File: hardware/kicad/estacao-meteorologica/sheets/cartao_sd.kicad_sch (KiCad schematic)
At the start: 7 parts, among them J17 Micro_SD_Card, U11 74LVC125

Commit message: refatoracao: atualizacoes de hardware e falta revisao LoRa
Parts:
- removed C9: 10u, symbol Device:C_Polarized
- added C7: 10u / 50V, Capacitor_SMD:C_1206_3216Metric, symbol Device:C
- added C9: 100n, Capacitor_SMD:C_0603_1608Metric, symbol Device:C
- added U39: EMIF06-MSD02N16, Hardware_SD:QFN-16L_L3.5-W1.2-P0.40_EMIF06-MSD02N16, symbol Hardware_SD:EMIF06-MSD02N16
- C10, C8: footprint (none) -> Capacitor_SMD:C_0603_1608Metric; LCSC (none) -> C14663; LCSC Part (none) -> C14663; MPN (none) -> CC0603KRX7R9BB104; Manufacturer (none) -> YAGEO; Rating (none) -> X7R; 100 nF; 50 V; ±10 %; 0603
- J17: value Micro_SD_Card -> 104031-0811; MPN (none) -> 104031-0811; Manufacturer (none) -> Molex; Rating (none) -> 10 V; 0.5 A; -25 °C to +85 °C; SMT
- R17, R18: footprint (none) -> Resistor_SMD:R_0603_1608Metric; LCSC (none) -> C25804; LCSC Part (none) -> C25804; MPN (none) -> 0603WAF1002T5E; Manufacturer (none) -> UNI-ROYAL; Rating (none) -> 10 kOhm; ±1 %; 0.1 W; 0603
- U11: value 74LVC125 -> SN74LVC125APWR; LCSC (none) -> C7813; LCSC Part (none) -> C7813; MPN (none) -> SN74LVC125APWR; Manufacturer (none) -> Texas Instruments; Rating (none) -> VCC 1.65 V to 3.6 V; 24 mA; TSSOP-14
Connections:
- net +5V is gone; now on net +3V3: C8.1, U11.14 (VCC)
- net +3V3: now also C7.1, C9.1, U39.16 (VCC), U39.17 (RDAT_VCC); no longer U11.7 (GND)
- net CS_LLS: now also U39.4 (DAT3_IN); no longer J17.2 (DAT3/CD)
- net DI_LLS: now also U39.5 (CMD_IN); no longer J17.3 (CMD)
- net DO_LLS: now also U39.7 (DAT0_IN); no longer J17.7 (DAT0)
- net GND: now also U11.7 (GND), C7.2, C9.2, U39.18 (GND), U39.19 (GND), U39.9 (GND)
- net SCK_LLS: now also U39.6 (CLK_IN); no longer J17.5 (CLK)
- net DAT2: now reaches J17.1 (DAT2)
- net DAT2: now also U39.15 (DAT2_EX)
- net DAT1: now reaches J17.8 (DAT1)
- net DAT1: now also U39.10 (DAT1_EX)
- new net D_CMD_CARD: J17.3 (CMD), U39.13 (CMD_EX)
- new net SD_CLK_CARD: J17.5 (CLK), U39.12 (CLK_EX)
- new net SD_CS_CARD: J17.2 (DAT3/CD), U39.14 (DAT3_EX)
- new net SD_DO_CARD: J17.7 (DAT0), U39.11 (DAT0_EX)
- no-connect marks 2 -> 4
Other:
- moved on the sheet: C8, J17, R17, R18, U11A, U11B, U11C, U11D, U11E

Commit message: refatoracao: lora + Verificacao projeto inteiro
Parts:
- C10, C8, C9: Modelo 3D (none) -> ${KICAD9_3DMODEL_DIR}/Capacitor_SMD.3dshapes/C_0603_1608Met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; Status_Ficha (none) -> Conferido no catalogo em 2026-09-24; verificar estoque ao c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
- C7: Modelo 3D (none) -> ${KICAD9_3DMODEL_DIR}/Capacitor_SMD.3dshapes/C_1206_3216Met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; Status_Ficha (none) -> Conferido no catalogo em 2026-09-24; verificar estoque ao c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
- J17: LCSC (none) -> Nao confirmado; LCSC Part (none) -> Nao confirmado; Modelo 3D (none) -> PENDENTE: ${KICAD9_3DMODEL_DIR}/Connector_Card.3dshapes/mic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; Status_Ficha (none) -> MPN e geometria preservados; fornecimento LCSC nao confirma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
- R17, R18: Modelo 3D (none) -> ${KICAD9_3DMODEL_DIR}/Resistor_SMD.3dshapes/R_0603_1608Metr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; Status_Ficha (none) -> Conferido no catalogo em 2026-09-24; verificar estoque ao c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
- U11: Modelo 3D (none) -> ${KICAD9_3DMODEL_DIR}/Package_SO.3dshapes/TSSOP-14_4.4x5mm_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; Status_Ficha (none) -> Conferido no catalogo em 2026-09-24; verificar estoque ao c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
- U39: Modelo 3D (none) -> ${KIPRJMOD}/../../libraries/Hardware_SD/Hardware_SD.3dshape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; Status_Ficha (none) -> Conferido no catalogo em 2026-09-24; verificar estoque ao c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
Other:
- moved on the sheet: C7, C9

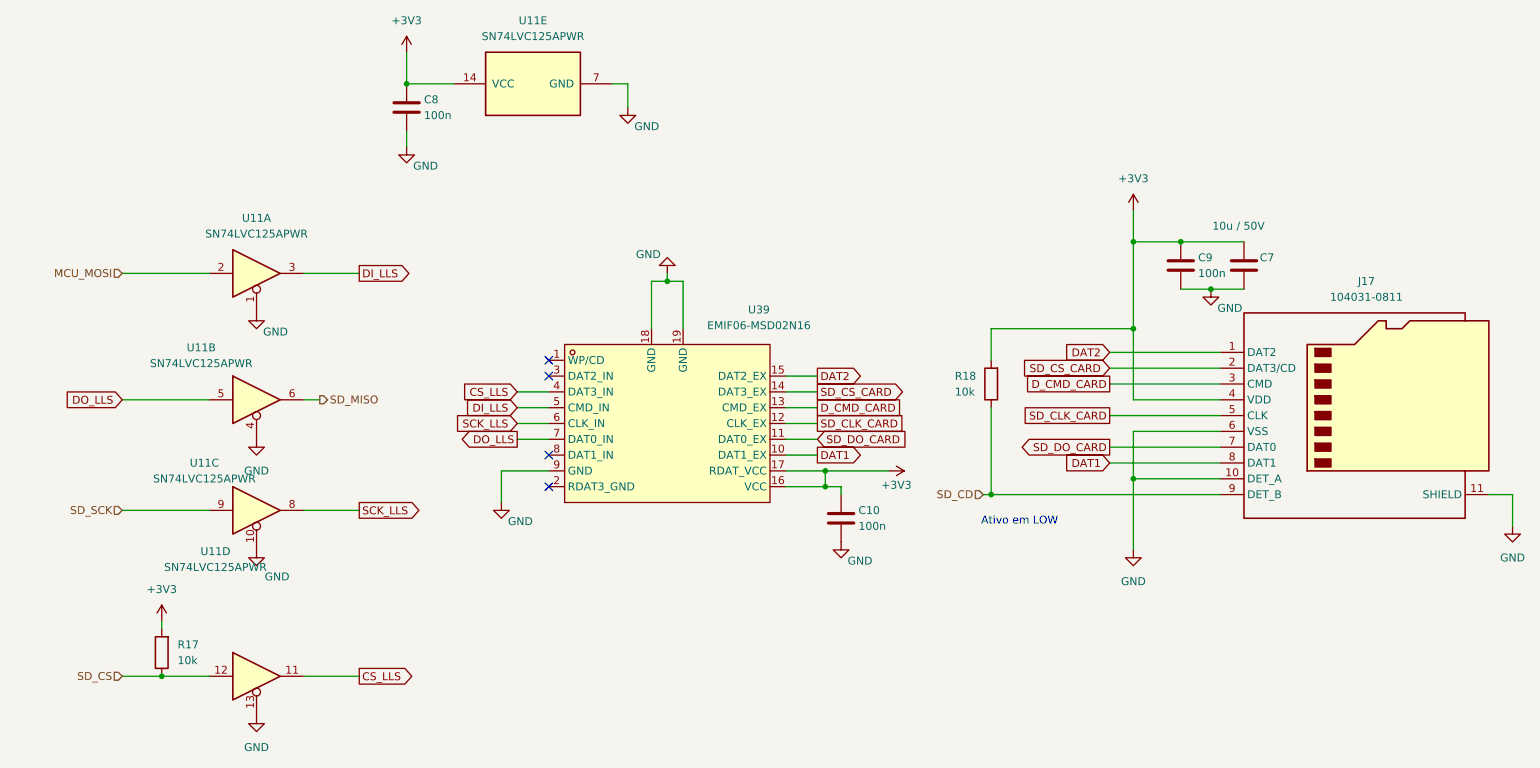
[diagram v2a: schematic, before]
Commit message: Padronizacao de nomes e numero de componentes
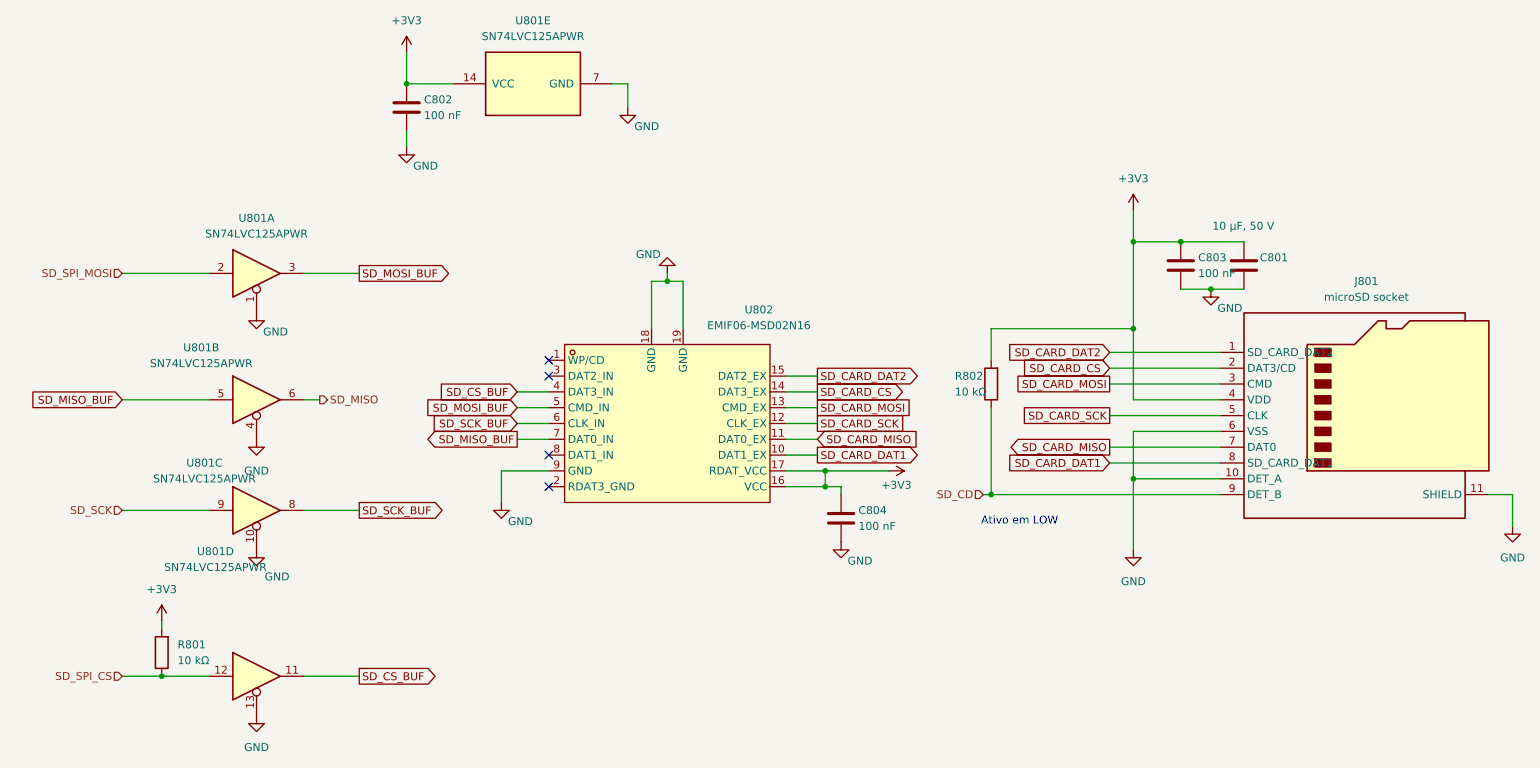
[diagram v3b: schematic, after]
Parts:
- C801: renamed from C7; value 10u / 50V -> 10 µF, 50 V; Assembly (none) -> SMT; Function (none) -> Capacitor de desacoplamento ou filtro local.; LCSC Part C13585 -> (none); Modelo 3D ${KICAD9_3DMODEL_DIR}/Capacitor_SMD.3dshapes/C_1206_3216Met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 -> (none); Rating X5R; 10 uF; 50 V; ±10 %; 1206 -> (none); Specification (none) -> X5R; 10 uF; 50 V; ±10 %; 1206; Status_Ficha Conferido no catalogo em 2026-09-24; verificar estoque ao c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 -> (none); Verification (none) -> Conferido no catalogo em 2026-09-24; verificar estoque ao c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
- C802: renamed from C8; value 100n -> 100 nF; Assembly (none) -> SMT; Function (none) -> Capacitor de desacoplamento ou filtro local.; LCSC Part C14663 -> (none); Modelo 3D ${KICAD9_3DMODEL_DIR}/Capacitor_SMD.3dshapes/C_0603_1608Met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 -> (none); Rating X7R; 100 nF; 50 V; ±10 %; 0603 -> (none); Specification (none) -> X7R; 100 nF; 50 V; ±10 %; 0603; Status_Ficha Conferido no catalogo em 2026-09-24; verificar estoque ao c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 -> (none); Verification (none) -> Conferido no catalogo em 2026-09-24; verificar estoque ao c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
- C803: renamed from C9; value 100n -> 100 nF; Assembly (none) -> SMT; Function (none) -> Capacitor de desacoplamento ou filtro local.; LCSC Part C14663 -> (none); Modelo 3D ${KICAD9_3DMODEL_DIR}/Capacitor_SMD.3dshapes/C_0603_1608Met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 -> (none); Rating X7R; 100 nF; 50 V; ±10 %; 0603 -> (none); Specification (none) -> X7R; 100 nF; 50 V; ±10 %; 0603; Status_Ficha Conferido no catalogo em 2026-09-24; verificar estoque ao c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 -> (none); Verification (none) -> Conferido no catalogo em 2026-09-24; verificar estoque ao c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
- C804: renamed from C10; value 100n -> 100 nF; Assembly (none) -> SMT; Function (none) -> Capacitor de desacoplamento ou filtro local.; LCSC Part C14663 -> (none); Modelo 3D ${KICAD9_3DMODEL_DIR}/Capacitor_SMD.3dshapes/C_0603_1608Met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 -> (none); Rating X7R; 100 nF; 50 V; ±10 %; 0603 -> (none); Specification (none) -> X7R; 100 nF; 50 V; ±10 %; 0603; Status_Ficha Conferido no catalogo em 2026-09-24; verificar estoque ao c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 -> (none); Verification (none) -> Conferido no catalogo em 2026-09-24; verificar estoque ao c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
- J801: renamed from J17; value 104031-0811 -> microSD socket; Assembly (none) -> SMT; Function (none) -> Conector de interface.; LCSC Part Nao confirmado -> (none); Modelo 3D PENDENTE: ${KICAD9_3DMODEL_DIR}/Connector_Card.3dshapes/mic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 -> (none); Rating 10 V; 0.5 A; -25 °C to +85 °C; SMT -> (none); Specification (none) -> 10 V; 0.5 A; -25 °C to +85 °C; SMT; Status_Ficha MPN e geometria preservados; fornecimento LCSC nao confirma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 -> (none); Verification (none) -> MPN e geometria preservados; fornecimento LCSC nao confirma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
- R801: renamed from R17; value 10k -> 10 kΩ; Assembly (none) -> SMT; Function (none) -> Resistor de polarização, filtro ou configuração.; LCSC Part C25804 -> (none); Manufacturer UNI-ROYAL -> UNI-ROYAL(Uniroyal Elec); Modelo 3D ${KICAD9_3DMODEL_DIR}/Resistor_SMD.3dshapes/R_0603_1608Metr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 -> (none); Rating 10 kOhm; ±1 %; 0.1 W; 0603 -> (none); Specification (none) -> 10 kOhm; ±1 %; 0.1 W; 0603; Status_Ficha Conferido no catalogo em 2026-09-24; verificar estoque ao c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 -> (none); Verification (none) -> Conferido no catalogo em 2026-09-24; verificar estoque ao c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
- R802: renamed from R18; value 10k -> 10 kΩ; Assembly (none) -> SMT; Function (none) -> Resistor de polarização, filtro ou configuração.; LCSC Part C25804 -> (none); Manufacturer UNI-ROYAL -> UNI-ROYAL(Uniroyal Elec); Modelo 3D ${KICAD9_3DMODEL_DIR}/Resistor_SMD.3dshapes/R_0603_1608Metr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 -> (none); Rating 10 kOhm; ±1 %; 0.1 W; 0603 -> (none); Specification (none) -> 10 kOhm; ±1 %; 0.1 W; 0603; Status_Ficha Conferido no catalogo em 2026-09-24; verificar estoque ao c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 -> (none); Verification (none) -> Conferido no catalogo em 2026-09-24; verificar estoque ao c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
- U801: renamed from U11; Assembly (none) -> SMT; Function (none) -> Circuito integrado ou módulo funcional.; LCSC Part C7813 -> (none); Modelo 3D ${KICAD9_3DMODEL_DIR}/Package_SO.3dshapes/TSSOP-14_4.4x5mm_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 -> (none); Rating VCC 1.65 V to 3.6 V; 24 mA; TSSOP-14 -> (none); Specification (none) -> VCC 1.65 V to 3.6 V; 24 mA; TSSOP-14; Status_Ficha Conferido no catalogo em 2026-09-24; verificar estoque ao c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 -> (none); Verification (none) -> Conferido no catalogo em 2026-09-24; verificar estoque ao c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
- U802: renamed from U39; 3D Model ${KIPRJMOD}/../../libraries/Hardware_SD/Hardware_SD.3dshape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 -> (none); Assembly (none) -> SMT; Function (none) -> Circuito integrado ou módulo funcional.; LCSC Part C5267594 -> (none); Modelo 3D ${KIPRJMOD}/../../libraries/Hardware_SD/Hardware_SD.3dshape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 -> (none); Rating 6 channels; 45 Ohm series; 20 pF; IEC 61000-4-2 level 4 -> (none); Specification (none) -> 6 channels; 45 Ohm series; 20 pF; IEC 61000-4-2 level 4; Status_Ficha Conferido no catalogo em 2026-09-24; verificar estoque ao c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 -> (none); Verification (none) -> Conferido no catalogo em 2026-09-24; verificar estoque ao c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
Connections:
- net CS_LLS renamed SD_CS_BUF
- net DAT1 renamed SD_CARD_DAT1
- net DAT2 renamed SD_CARD_DAT2
- net DI_LLS renamed SD_MOSI_BUF
- net DO_LLS renamed SD_MISO_BUF
- net D_CMD_CARD renamed SD_CARD_MOSI
- net MCU_MOSI renamed SD_SPI_MOSI
- net SCK_LLS renamed SD_SCK_BUF
- net SD_CLK_CARD renamed SD_CARD_SCK
- net SD_CS renamed SD_SPI_CS
- net SD_CS_CARD renamed SD_CARD_CS
- net SD_DO_CARD renamed SD_CARD_MISO

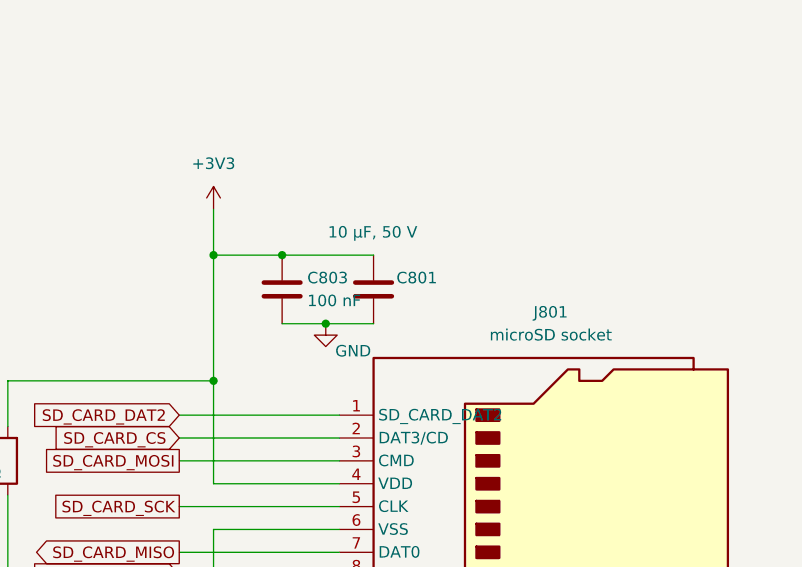
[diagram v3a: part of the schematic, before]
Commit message: Ajuste de componentes por folha
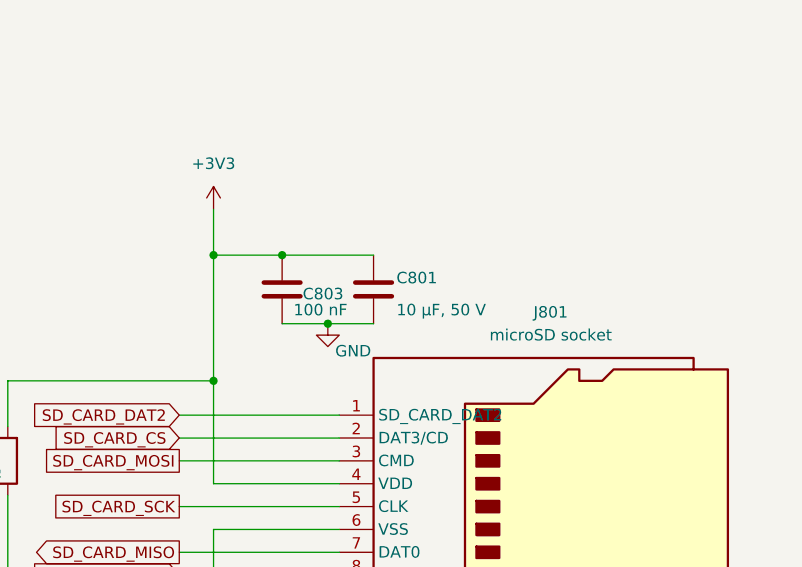
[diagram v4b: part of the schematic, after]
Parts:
- J801: footprint Connector_Card:microSD_HC_Molex_104031-0811 -> Hardware_SD_Interface:microSD_HC_Molex_104031-0811; symbol Connector:Micro_SD_Card_Det2 -> Hardware_SD_Interface:MicroSD_Molex_104031_0811; LCSC Nao confirmado -> C585350; LCSC Part (none) -> C585350; Modelo 3D (none) -> ${KIPRJMOD}/../../libraries/Hardware_SD_Interface/Hardware_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; Verification MPN e geometria preservados; fornecimento LCSC nao confirma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 -> Conferido no catálogo da JLCPCB em 2026-09-25; C585350; con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
- U801: symbol 74xx:74LVC125 -> Hardware_SD_Interface:SN74LVC125APWR

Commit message: Roteamento 1
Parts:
- J801: value microSD socket -> microSD socket, TF-15x15; footprint Hardware_SD_Interface:microSD_HC_Molex_104031-0811 -> Hardware_SD_Interface:microSD_SOFNG_TF-15x15; Function Conector de interface. -> Socket microSD para armazenamento SPI; contatos 1-8 e detec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; LCSC C585350 -> C111196; LCSC Part C585350 -> (none); MPN 104031-0811 -> TF-15x15; Manufacturer Molex -> SOFNG; Modelo 3D ${KIPRJMOD}/../../libraries/Hardware_SD_Interface/Hardware_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 -> (none); Specification 10 V; 0.5 A; -25 °C to +85 °C; SMT -> 25 mA; 24 VDC; -25 °C a +85 °C; 6500 ciclos sem carga; SMD; Verification Conferido no catálogo da JLCPCB em 2026-09-25; C585350; con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 -> Footprint conferido no datasheet SOFNG/LCSC C111196 em 2026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
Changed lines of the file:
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@@
 			)
 		)
-		(property "Value" "microSD socket"
+		(property "Value" "microSD socket, TF-15x15"
 			(at 240.665 66.04 0)
 			(effects
@@
 			)
 		)
-		(property "Footprint" "Hardware_SD_Interface:microSD_HC_Molex_104031-0811"
+		(property "Footprint" "Hardware_SD_Interface:microSD_SOFNG_TF-15x15"
 			(at 292.1 67.31 0)
 			(effects
@@
 			)
 		)
-		(property "Datasheet" "https://www.molex.com/content/dam/molex/molex-dot-com/products/automated/en-us/productspecificationpdf/104/104031/PS-104031-001-001.pdf?inline="
+		(property "Datasheet" "https://datasheet.lcsc.com/datasheet/pdf/38dcce1bae4dd4ca995533b0c0352a82.pdf?productCode=C111196"
 			(at 242.57 82.55 0)
 			(effects
@@
 			)
 		)
-		(property "Description" "Molex microSD socket, push-pull, SMT, 1.42 mm height, mechanical card-detect"
+		(property "Description" "SOFNG TF-15x15, socket microSD SMD push-push, 14.50 x 14.75 x 1.90 mm, com detecção mecânica"
 			(at 240.03 85.09 0)
 			(effects
@@
 			)
 		)
-		(property "MPN" "104031-0811"
+		(property "MPN" "TF-15x15"
 			(at 36.83 10.16 0)
 			(effects
@@
 			)
 		)
-		(property "Specification" "10 V; 0.5 A; -25 °C to +85 °C; SMT"
+		(property "Specification" "25 mA; 24 VDC; -25 °C a +85 °C; 6500 ciclos sem carga; SMD"
 			(at 36.83 10.16 0)
 			(effects
@@
 			)
 		)
-		(property "Manufacturer" "Molex"
+		(property "Manufacturer" "SOFNG"
 			(at 36.83 10.16 0)
 			(effects
@@
 			)
 		)
-		(property "LCSC" "C585350"
+		(property "LCSC" "C111196"
 			(at 240.03 85.09 0)
 			(effects
@@
 			)
 		)
-		(property "Verification" "Conferido no catálogo da JLCPCB em 2026-09-25; C585350; confirmar estoque antes da compra"
+		(property "Verification" "Footprint conferido no datasheet SOFNG/LCSC C111196 em 2026-09-26; confirmar estoque antes da compra"
 			(at 240.03 85.09 0)
 			(effects
@@
 			)
 		)
-		(property "LCSC Part" "C585350"
-			(at 240.03 85.09 0)
-			(effects
-				(font
-					(size 1.27 1.27)
-				)
-				(hide yes)
-			)
-		)
-		(property "Modelo 3D" "${KIPRJMOD}/../../libraries/Hardware_SD_Interface/Hardware_SD_Interface.3dshapes/1040310811.step"
-			(at 240.03 85.09 0)
-			(effects
-				(font
-					(size 1.27 1.27)
-				)
-				(hide yes)
-			)
-		)
-		(property "Function" "Conector de interface."
+		(property "Function" "Socket microSD para armazenamento SPI; contatos 1-8 e detecção mecânica."
 			(at 0 0 0)
 			(effects

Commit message: rotemento 3.0
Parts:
- J801: footprint Hardware_SD_Interface:microSD_SOFNG_TF-15x15 -> Hardware_SD_Interface:microSD_SOFNG_TF-15x15_C111196; symbol Hardware_SD_Interface:MicroSD_Molex_104031_0811 -> Hardware_SD_Interface:MicroSD_SOFNG_TF_15x15; Function Socket microSD para armazenamento SPI; contatos 1-8 e detec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 -> Socket microSD para armazenamento SPI; contatos 1-8, detecç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; Verification Footprint conferido no datasheet SOFNG/LCSC C111196 em 2026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 -> Footprint e modelo 3D importados do EDA model do SOFNG/LCSC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
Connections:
- net GND: now also J801.12 (SHIELD), J801.13 (SHIELD)
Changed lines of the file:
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@@
 	)
 	(symbol
-		(lib_id "Hardware_SD_Interface:MicroSD_Molex_104031_0811")
+		(lib_id "Hardware_SD_Interface:MicroSD_SOFNG_TF_15x15")
 		(at 240.03 85.09 0)
 		(unit 1)
@@
 			)
 		)
-		(property "Footprint" "Hardware_SD_Interface:microSD_SOFNG_TF-15x15"
+		(property "Footprint" "Hardware_SD_Interface:microSD_SOFNG_TF-15x15_C111196"
 			(at 292.1 67.31 0)
 			(effects
@@
 			)
 		)
-		(property "Verification" "Footprint conferido no datasheet SOFNG/LCSC C111196 em 2026-09-26; confirmar estoque antes da compra"
+		(property "Verification" "Footprint e modelo 3D importados do EDA model do SOFNG/LCSC C111196 e confrontados com o datasheet em 2026-09-28; confirmar estoque antes da compra"
 			(at 240.03 85.09 0)
 			(effects
@@
 			)
 		)
-		(property "Function" "Socket microSD para armazenamento SPI; contatos 1-8 e detecção mecânica."
+		(property "Function" "Socket microSD para armazenamento SPI; contatos 1-8, detecção mecânica e três abas de blindagem aterradas."
 			(at 0 0 0)
 			(effects
@@
 		(pin "11"
 		)
+		(pin "12"
+		)
+		(pin "13"
+		)
 		(instances
